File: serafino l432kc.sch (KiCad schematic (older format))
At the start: 15 parts

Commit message: Avances
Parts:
- added C? (x2): 12p, symbol Device:C_Small
- added R?: R_Small, symbol Device:R_Small
- added Y?: 16MHz, symbol Device:Crystal_GND24_Small
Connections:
- wire segments 59 -> 79
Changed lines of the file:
@@
 	0    -1   -1   0
 $EndComp
+$Comp
+L Device:Crystal_GND24_Small Y?
+U 1 1 5FC74273
+P 3000 4100
+F 0 "Y?" H 2950 4550 50  0000 L CNN
+F 1 "16MHz" H 2850 4450 50  0000 L CNN
+F 2 "" H 3000 4100 50  0001 C CNN
+F 3 "~" H 3000 4100 50  0001 C CNN
+	1    3000 4100
+	1    0    0    -1
+$EndComp
+$Comp
+L Device:C_Small C?
+U 1 1 5FC752BD
+P 3300 4250
+F 0 "C?" H 3392 4296 50  0000 L CNN
+F 1 "12p" H 3392 4205 50  0000 L CNN
+F 2 "" H 3300 4250 50  0001 C CNN
+F 3 "~" H 3300 4250 50  0001 C CNN
+	1    3300 4250
+	1    0    0    -1
+$EndComp
+$Comp
+L Device:C_Small C?
+U 1 1 5FC75AB7
+P 2700 4250
+F 0 "C?" H 2500 4300 50  0000 L CNN
+F 1 "12p" H 2500 4200 50  0000 L CNN
+F 2 "" H 2700 4250 50  0001 C CNN
+F 3 "~" H 2700 4250 50  0001 C CNN
+	1    2700 4250
+	1    0    0    -1
+$EndComp
+Wire Wire Line
+	2700 4350 2700 4500
+Wire Wire Line
+	2700 4500 3000 4500
+Wire Wire Line
+	3300 4500 3300 4350
+$Comp
+L Device:R_Small R?
+U 1 1 5FC77AD8
+P 3300 3900
+F 0 "R?" H 3241 3854 50  0000 R CNN
+F 1 "R_Small" H 3241 3945 50  0000 R CNN
+F 2 "" H 3300 3900 50  0001 C CNN
+F 3 "~" H 3300 3900 50  0001 C CNN
+	1    3300 3900
+	-1   0    0    1
+$EndComp
+Wire Wire Line
+	3300 4000 3300 4100
+Wire Wire Line
+	2700 4150 2700 4100
+Wire Wire Line
+	2700 4100 2900 4100
+Wire Wire Line
+	3100 4100 3300 4100
+Connection ~ 3300 4100
+Wire Wire Line
+	3300 4100 3300 4150
+Wire Wire Line
+	3000 4200 3000 4300
+Connection ~ 3000 4500
+Wire Wire Line
+	3000 4500 3300 4500
+$Comp
+L power:GND #PWR?
+U 1 1 5FC7CF86
+P 3000 4650
+F 0 "#PWR?" H 3000 4400 50  0001 C CNN
+F 1 "GND" H 3005 4477 50  0000 C CNN
+F 2 "" H 3000 4650 50  0001 C CNN
+F 3 "" H 3000 4650 50  0001 C CNN
+	1    3000 4650
+	1    0    0    -1
+$EndComp
+Wire Wire Line
+	3000 4650 3000 4500
+Wire Wire Line
+	3000 4000 3000 3900
+Wire Wire Line
+	3000 3900 3150 3900
+Wire Wire Line
+	3150 3900 3150 4300
+Wire Wire Line
+	3150 4300 3000 4300
+Connection ~ 3000 4300
+Wire Wire Line
+	3000 4300 3000 4500
+Text GLabel 3400 3550 2    50   Input ~ 0
+HSE_IN
+Wire Wire Line
+	2700 4100 2700 3550
+Connection ~ 2700 4100
+Text GLabel 3400 3650 2    50   Input ~ 0
+HSE_OUT
+Wire Wire Line
+	3400 3650 3300 3650
+Wire Wire Line
+	3300 3650 3300 3800
+Wire Wire Line
+	2700 3550 3400 3550
 $EndSCHEMATC

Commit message: Working on the power supply
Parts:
- removed C? (x2): 12p, symbol Device:C_Small
- removed D?: B5B19W, symbol Device:D_Schottky_Small
- removed F?: 500mA, symbol Device:Fuse_Small
- removed FB?: 100@100MHz, symbol Device:Ferrite_Bead_Small
- removed R?: R_Small, symbol Device:R_Small
- removed Y?: 16MHz, symbol Device:Crystal_GND24_Small
- added C? (x2): 4.3pF, symbol Device:C_Small
- added C?: 100nF, symbol Device:C_Small
- added D?: BLUE, symbol Device:LED_Small
- added F?: 500mA, symbol Device:Polyfuse_Small
- added L?: 39h, symbol Device:L_Small
- added Q?: AO3401A, Package_TO_SOT_SMD:SOT-23, symbol Transistor_FET:AO3401A
- added R?: 1.5K, symbol Device:R_Small
- added SW?: SW_Push, symbol Switch:SW_Push
- added Y?: 32.768K, symbol Device:Crystal_Small
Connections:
- net labels added: +6V, LED0
- wire segments 79 -> 83

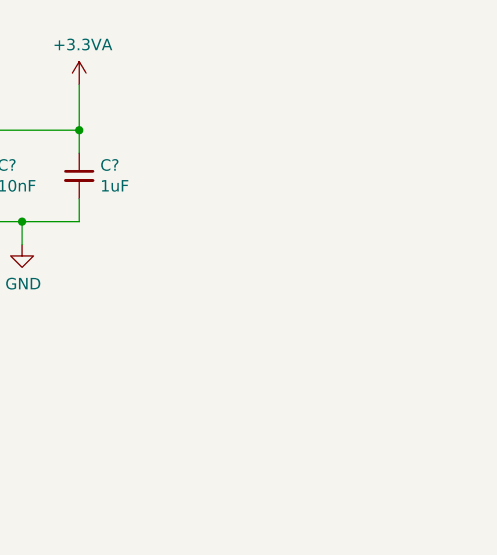
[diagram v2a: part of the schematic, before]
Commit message: Add MP2359DJ Buck Converter to Serafino Lib
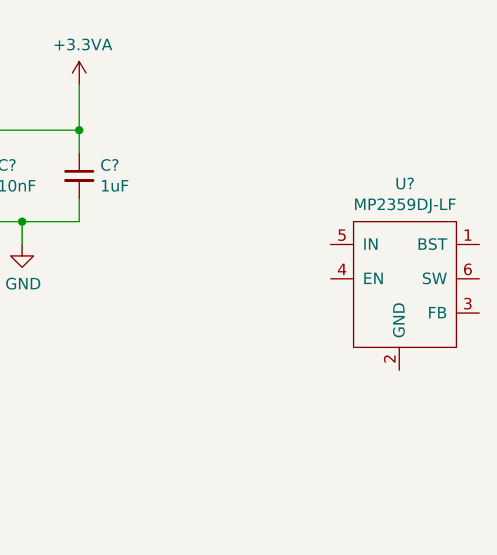
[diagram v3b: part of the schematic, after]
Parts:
- added U?: MP2359DJ-LF, symbol serafino:MP2359DJ-LF
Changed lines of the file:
@@
+	1    0    0    -1
+$EndComp
+$Comp
+L serafino:MP2359DJ-LF U?
+U 1 1 5FCA7BE3
+P 9400 2050
+F 0 "U?" H 9425 2465 50  0000 C CNN
+F 1 "MP2359DJ-LF" H 9425 2374 50  0000 C CNN
+F 2 "" H 9350 2100 50  0001 C CNN
+F 3 "" H 9350 2100 50  0001 C CNN
+	1    9400 2050
 	1    0    0    -1
 $EndComp

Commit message: avances...
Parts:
- added C?: 10uF, symbol Device:C_Small
- added C?: 10nF, symbol Device:C_Small
- added D?: B5819W, symbol Device:D_Schottky_Small
- added F?: 500mA, symbol Device:Polyfuse_Small
- added FB?: 600@600MHz, symbol Device:Ferrite_Bead_Small
- added L?: 10uH, symbol Device:L_Small
- added Q?: AO3401A, Package_TO_SOT_SMD:SOT-23, symbol Transistor_FET:AO3401A
- added R?: 100k, symbol Device:R_Small
- added R?: 68k, symbol Device:R_Small
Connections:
- net GND: now also U?.2 (GND), C?.2, D?.2 (A), Q?.1 (G)
- net BUCK_BST: now reaches U?.1 (BST)
- net BUCK_BST: now also C?.1
- net BUCK_FB: now reaches U?.3 (FB)
- net BUCK_EN: now reaches U?.4 (EN)
- net BUCK_EN: now also R?.1, R?.2
- net BUCK_IN: now reaches U?.5 (IN)
- net BUCK_IN: now also C?.1, FB?.2, R?.1
- net BUCK_SW: now reaches U?.6 (SW)
- net BUCK_SW: now also C?.2, D?.1 (K)
- new net: F?.1, Q?.3 (D)
- new net: FB?.1, Q?.2 (S)
- new net +12V: F?.2
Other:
- moved on the sheet: C?, D?, F?, FB?, L?, Q?, R?, SW?, U?, Y?

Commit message: Avances
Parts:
- added C? (x2): 10uF, symbol Device:C_Small
- added D?: B5819W, symbol Device:D_Schottky_Small
- added J?: USB_B_Micro, symbol Connector:USB_B_Micro
- added R?: 47k, symbol Device:R_Small
- added R?: 15k, symbol Device:R_Small
- added R?: 270, symbol Device:R_Small
- added U?: USBLC6-2SC6, Package_TO_SOT_SMD:SOT-23-6, symbol Power_Protection:USBLC6-2SC6
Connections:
- net BUCK_SW is gone; now on an unnamed net: C?.2, D?.1 (K), U?.6 (SW)
- net +3V3: now also L?.2, C?.1, C?.1, R?.1
- net GND: now also R?.2, C?.2, C?.2, R?.2
- net at FB?.1, Q?.2 (S): now also D?.1 (K)
- net BUCK_BST: no longer names the net of C?.1, U?.1 (BST)
- net BUCK_EN: no longer names the net of R?.1, R?.2, U?.4 (EN)
- net BUCK_FB: no longer names the net of U?.3 (FB)
- net BUCK_FB: now also R?.1, R?.2
- net BUCK_IN: no longer names the net of C?.1, FB?.2, R?.1, U?.5 (IN)
- new net: R?.1, R?.2
- new net +5V: D?.2 (A), J?.1 (VBUS)
- no-connect marks 0 -> 1
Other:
- moved on the sheet: C?, D?, F?, FB?, L?, Q?, R?, SW?, U?

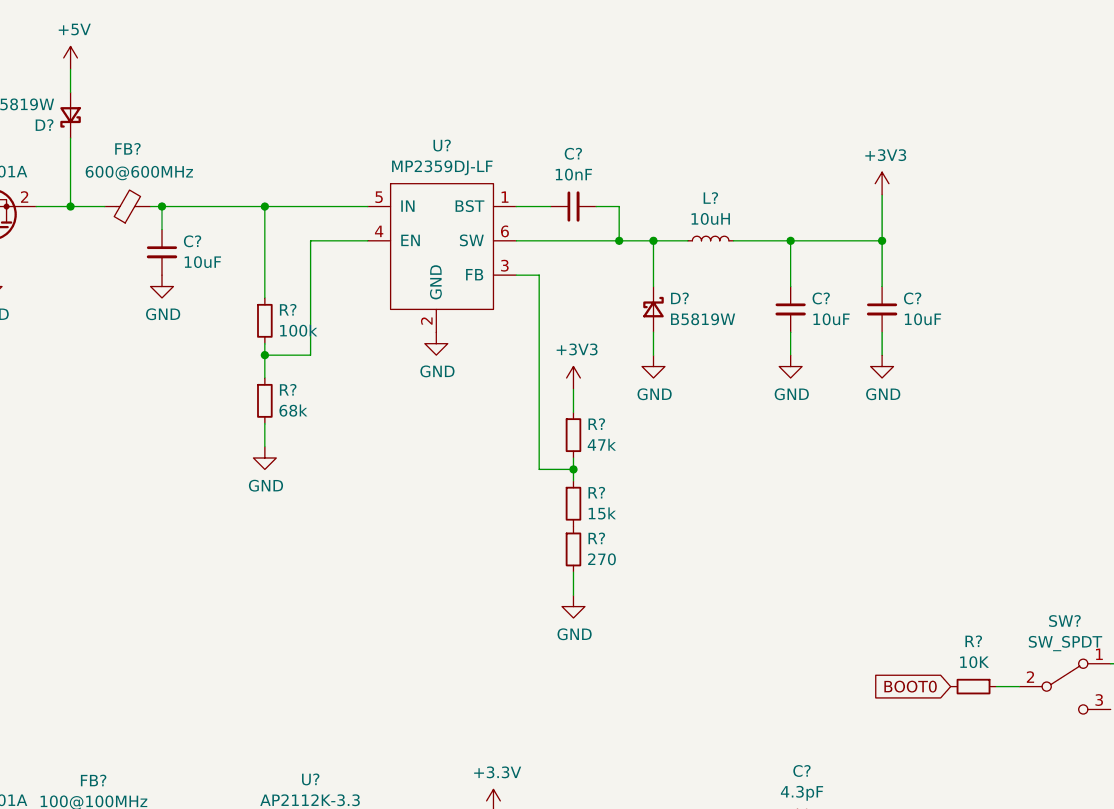
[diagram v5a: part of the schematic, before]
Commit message: Cambio de Power Supply
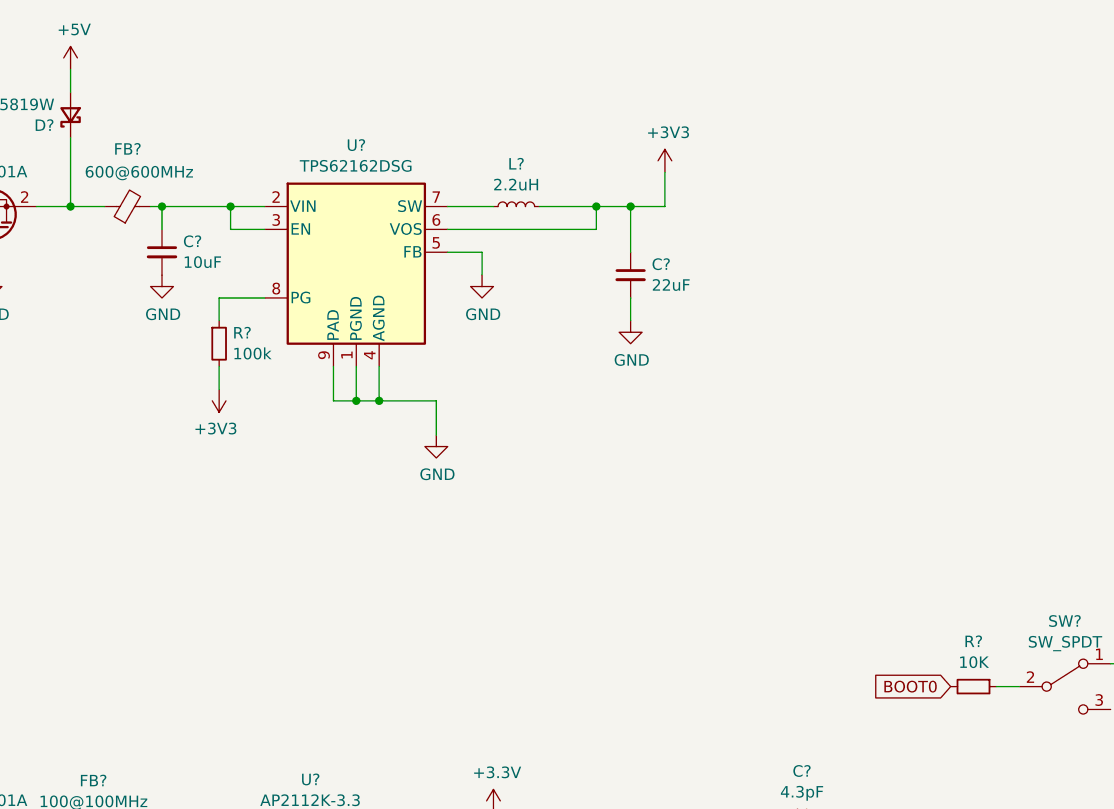
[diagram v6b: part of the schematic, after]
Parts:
- removed C? (x2): 10uF, symbol Device:C_Small
- removed C?: 10nF, symbol Device:C_Small
- removed D?: B5819W, symbol Device:D_Schottky_Small
- removed L?: 10uH, symbol Device:L_Small
- removed R?: 100k, symbol Device:R_Small
- removed R?: 68k, symbol Device:R_Small
- removed R?: 47k, symbol Device:R_Small
- removed R?: 15k, symbol Device:R_Small
- removed R?: 270, symbol Device:R_Small
- removed U?: MP2359DJ-LF, symbol serafino:MP2359DJ-LF
- added C?: 22uF, symbol Device:C_Small
- added L?: 2.2uH, symbol Device:L_Small
- added R?: 100k, symbol Device:R_Small
- added U?: TPS62162DSG, Package_SON:WSON-8-1EP_2x2mm_P0.5mm_EP0.9x1.6mm_ThermalVias, symbol Regulator_Switching:TPS62162DSG
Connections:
- net +3V3: now also C?.1, L?.2, R?.2, U?.6 (VOS)
- net GND: now also C?.2, U?.1 (PGND), U?.4 (AGND), U?.5 (FB), U?.9 (PAD)
- net at C?.1, FB?.2: now also U?.2 (VIN), U?.3 (EN)
- new net: L?.1, U?.7 (SW)
- new net: R?.1, U?.8 (PG)

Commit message: Updated pins
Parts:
- removed C? (x2): 10uF, symbol Device:C
- removed F?: 500mA, symbol Device:Polyfuse_Small
- removed FB?: 100@100MHz, symbol Device:Ferrite_Bead_Small
- removed Q?: AO3401A, Package_TO_SOT_SMD:SOT-23, symbol Transistor_FET:AO3401A
- removed U?: AP2112K-3.3, Package_TO_SOT_SMD:SOT-23-5, symbol Regulator_Linear:AP2112K-3.3
- added U?: MCP73831-2-OT, Package_TO_SOT_SMD:SOT-23-5, symbol Battery_Management:MCP73831-2-OT
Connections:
- net LED0: no longer U?.26 (PB3)
- net SAI1_FS_B: now reaches U?.10 (PA4)
- net SPI1_MISO: now reaches U?.12 (PA6)
- net SPI1_MOSI: now reaches U?.13 (PA7)
- net SPI1_SS: now reaches U?.14 (PB0)
- net SPI1_SCK: now reaches U?.7 (PA1)
- net USART2_TX: now reaches U?.8 (PA2)
- net USART2_RX: now reaches U?.9 (PA3)
- net USART1_RX renamed I2C1_SDA
- net USART1_TX renamed I2C1_SCL
- new net SAI1_SCK_B: U?.26 (PB3)
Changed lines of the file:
@@
 Text GLabel 9100 4900 2    50   Input ~ 0
 USB_D-
-Text GLabel 9100 4700 2    50   Input ~ 0
-USART1_TX
-Text GLabel 9100 4800 2    50   Input ~ 0
-USART1_RX
+Text GLabel 9100 4000 2    50   Input ~ 0
+USART2_TX
+Text GLabel 9100 4100 2    50   Input ~ 0
+USART2_RX
 Text Notes 7000 1150 0    50   ~ 0
 VDD Decouples
@@
 Wire Wire Line
 	4750 4550 5050 4550
-Text GLabel 8100 4900 0    50   Input ~ 0
-LED0
 $Comp
 L Device:LED_Small D?
@@
 	1800 5850 1700 5850
 $Comp
-L power:GND #PWR?
-U 1 1 5FCE6EE0
-P 1600 4400
-F 0 "#PWR?" H 1600 4150 50  0001 C CNN
-F 1 "GND" H 1605 4227 50  0000 C CNN
-F 2 "" H 1600 4400 50  0001 C CNN
-F 3 "" H 1600 4400 50  0001 C CNN
-	1    1600 4400
-	1    0    0    -1
-$EndComp
-Wire Wire Line
-	1800 4100 1950 4100
-Wire Wire Line
-	1300 4100 1400 4100
-$Comp
-L Transistor_FET:AO3401A Q?
-U 1 1 5FCDAB66
-P 1600 4200
-F 0 "Q?" V 1942 4200 50  0000 C CNN
-F 1 "AO3401A" V 1851 4200 50  0000 C CNN
-F 2 "Package_TO_SOT_SMD:SOT-23" H 1800 4125 50  0001 L CIN
-F 3 "http://www.aosmd.com/pdfs/datasheet/AO3401A.pdf" H 1600 4200 50  0001 L CNN
-	1    1600 4200
-	0    -1   -1   0
-$EndComp
-Wire Wire Line
-	900  4100 1100 4100
-Wire Wire Line
-	900  3800 900  4100
-$Comp
-L power:+6V #PWR?
-U 1 1 5FCCC238
-P 900 3800
-F 0 "#PWR?" H 900 3650 50  0001 C CNN
-F 1 "+6V" H 915 3973 50  0000 C CNN
-F 2 "" H 900 3800 50  0001 C CNN
-F 3 "" H 900 3800 50  0001 C CNN
-	1    900  3800
-	1    0    0    -1
-$EndComp
-$Comp
-L Device:Polyfuse_Small F?
-U 1 1 5FCC5DE0
-P 1200 4100
-F 0 "F?" V 995 4100 50  0000 C CNN
-F 1 "500mA" V 1086 4100 50  0000 C CNN
-F 2 "" H 1250 3900 50  0001 L CNN
-F 3 "~" H 1200 4100 50  0001 C CNN
-	1    1200 4100
-	0    1    1    0
-$EndComp
-Wire Wire Line
-	3800 4100 3550 4100
-Wire Wire Line
-	3800 4000 3800 4100
-$Comp
-L power:+3.3V #PWR?
-U 1 1 5FC6B21F
-P 3800 4000
-F 0 "#PWR?" H 3800 3850 50  0001 C CNN
-F 1 "+3.3V" H 3815 4173 50  0000 C CNN
-F 2 "" H 3800 4000 50  0001 C CNN
-F 3 "" H 3800 4000 50  0001 C CNN
-	1    3800 4000
-	1    0    0    -1
-$EndComp
-Wire Wire Line
-	3550 4650 3000 4650
-Wire Wire Line
-	3550 4550 3550 4650
-Wire Wire Line
-	3000 4650 3000 4750
-Connection ~ 3000 4650
-Wire Wire Line
-	2400 4650 3000 4650
-Wire Wire Line
-	2400 4550 2400 4650
-Wire Wire Line
-	3550 4250 3550 4100
-Wire Wire Line
-	2400 4250 2400 4100
-Wire Wire Line
-	3000 4500 3000 4650
-Connection ~ 2400 4100
-Wire Wire Line
-	2150 4100 2400 4100
-Connection ~ 3550 4100
-Wire Wire Line
-	3300 4100 3550 4100
-$Comp
-L Device:C C?
-U 1 1 5FC663E8
-P 3550 4400
-F 0 "C?" H 3665 4446 50  0000 L CNN
-F 1 "10uF" H 3665 4355 50  0000 L CNN
-F 2 "" H 3588 4250 50  0001 C CNN
-F 3 "~" H 3550 4400 50  0001 C CNN
-	1    3550 4400
-	1    0    0    -1
-$EndComp
-$Comp
-L Device:C C?
-U 1 1 5FC65A47
-P 2400 4400
-F 0 "C?" H 2515 4446 50  0000 L CNN
-F 1 "10uF" H 2515 4355 50  0000 L CNN
-F 2 "" H 2438 4250 50  0001 C CNN
-F 3 "~" H 2400 4400 50  0001 C CNN
-	1    2400 4400
-	1    0    0    -1
-$EndComp
-Wire Wire Line
-	2400 4100 2600 4100
-Wire Wire Line
-	2600 4100 2700 4100
-Connection ~ 2600 4100
-Wire Wire Line
-	2600 4200 2600 4100
-Wire Wire Line
-	2700 4200 2600 4200
-$Comp
-L power:GND #PWR?
-U 1 1 5FC64217
-P 3000 4750
-F 0 "#PWR?" H 3000 4500 50  0001 C CNN
-F 1 "GND" H 3005 4577 50  0000 C CNN
-F 2 "" H 3000 4750 50  0001 C CNN
-F 3 "" H 3000 4750 50  0001 C CNN
-	1    3000 4750
-	1    0    0    -1
-$EndComp
-$Comp
-L Device:Ferrite_Bead_Small FB?
-U 1 1 5FC335B0
-P 2050 4100
-F 0 "FB?" V 2287 4100 50  0000 C CNN
-F 1 "100@100MHz" V 2196 4100 50  0000 C CNN
-F 2 "" V 1980 4100 50  0001 C CNN
-F 3 "~" H 2050 4100 50  0001 C CNN
-	1    2050 4100
-	0    -1   -1   0
-$EndComp
-$Comp
-L Regulator_Linear:AP2112K-3.3 U?
-U 1 1 5FC3C450
-P 3000 4200
-F 0 "U?" H 3000 4542 50  0000 C CNN
-F 1 "AP2112K-3.3" H 3000 4451 50  0000 C CNN
-F 2 "Package_TO_SOT_SMD:SOT-23-5" H 3000 4525 50  0001 C CNN
-F 3 "https://www.diodes.com/assets/Datasheets/AP2112.pdf" H 3000 4300 50  0001 C CNN
-	1    3000 4200
-	1    0    0    -1
-$EndComp
-$Comp
 L Regulator_Switching:TPS62162DSG U?
 U 1 1 5FCD6953
@@
 	3550 2200 3550 2350
 Connection ~ 3300 2200
+$Comp
+L Battery_Management:MCP73831-2-OT U?
+U 1 1 5FCDFC7C
+P 1550 3700
+F 0 "U?" H 1550 4181 50  0000 C CNN
+F 1 "MCP73831-2-OT" H 1550 4090 50  0000 C CNN
+F 2 "Package_TO_SOT_SMD:SOT-23-5" H 1600 3450 50  0001 L CIN
+F 3 "http://ww1.microchip.com/downloads/en/DeviceDoc/20001984g.pdf" H 1400 3650 50  0001 C CNN
+	1    1550 3700
+	1    0    0    -1
+$EndComp
+Text GLabel 9100 4500 2    50   Input ~ 0
+SPI1_MOSI
+Text GLabel 9100 3900 2    50   Input ~ 0
+SPI1_SCK
+Text GLabel 9100 4400 2    50   Input ~ 0
+SPI1_MISO
+Text GLabel 9100 4800 2    50   Input ~ 0
+I2C1_SDA
+Text GLabel 9100 4700 2    50   Input ~ 0
+I2C1_SCL
+Text GLabel 8100 4700 0    50   Input ~ 0
+SPI1_SS
+Text GLabel 8100 4900 0    50   Input ~ 0
+SAI1_SCK_B
+Text GLabel 9100 4200 2    50   Input ~ 0
+SAI1_FS_B
 $EndSCHEMATC
